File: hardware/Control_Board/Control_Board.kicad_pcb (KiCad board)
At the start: 4 copper layers, 100 x 100 mm, 0 parts

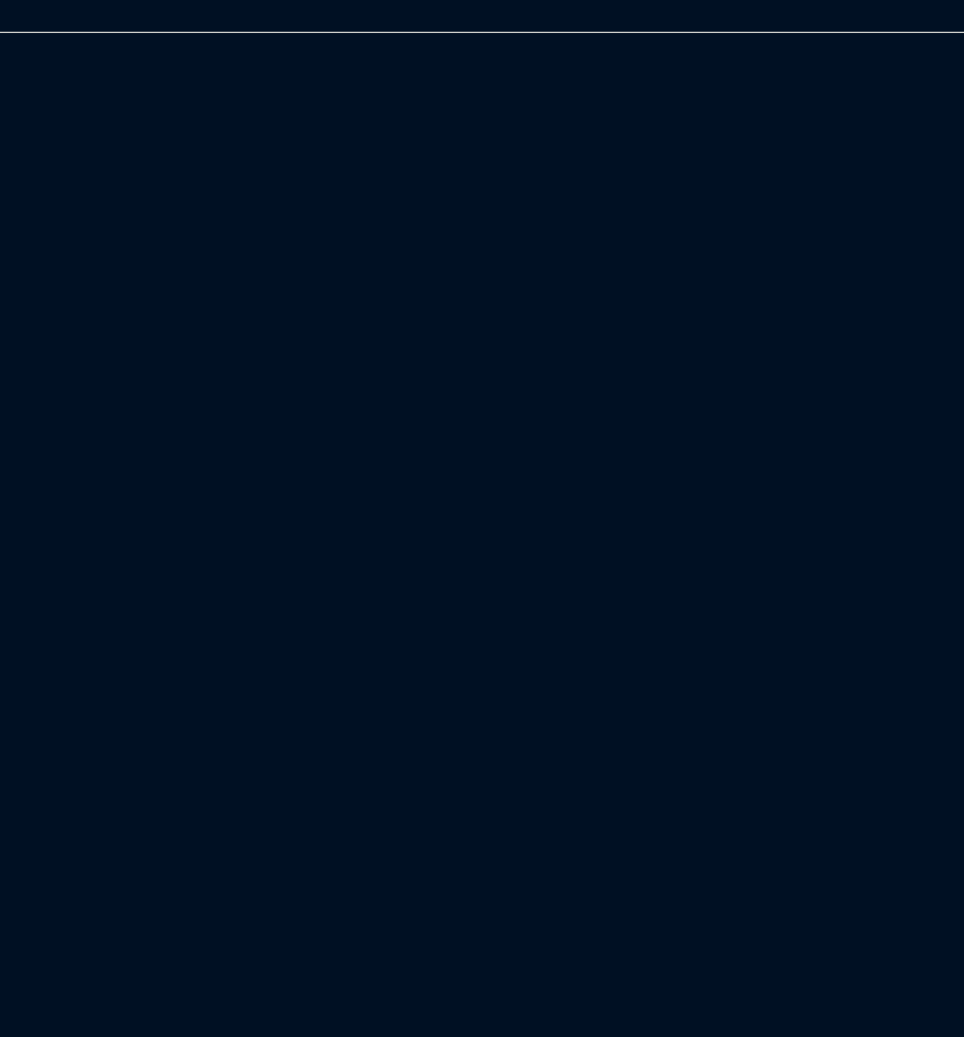
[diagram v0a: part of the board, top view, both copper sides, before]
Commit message: feat: update prototype with esp32
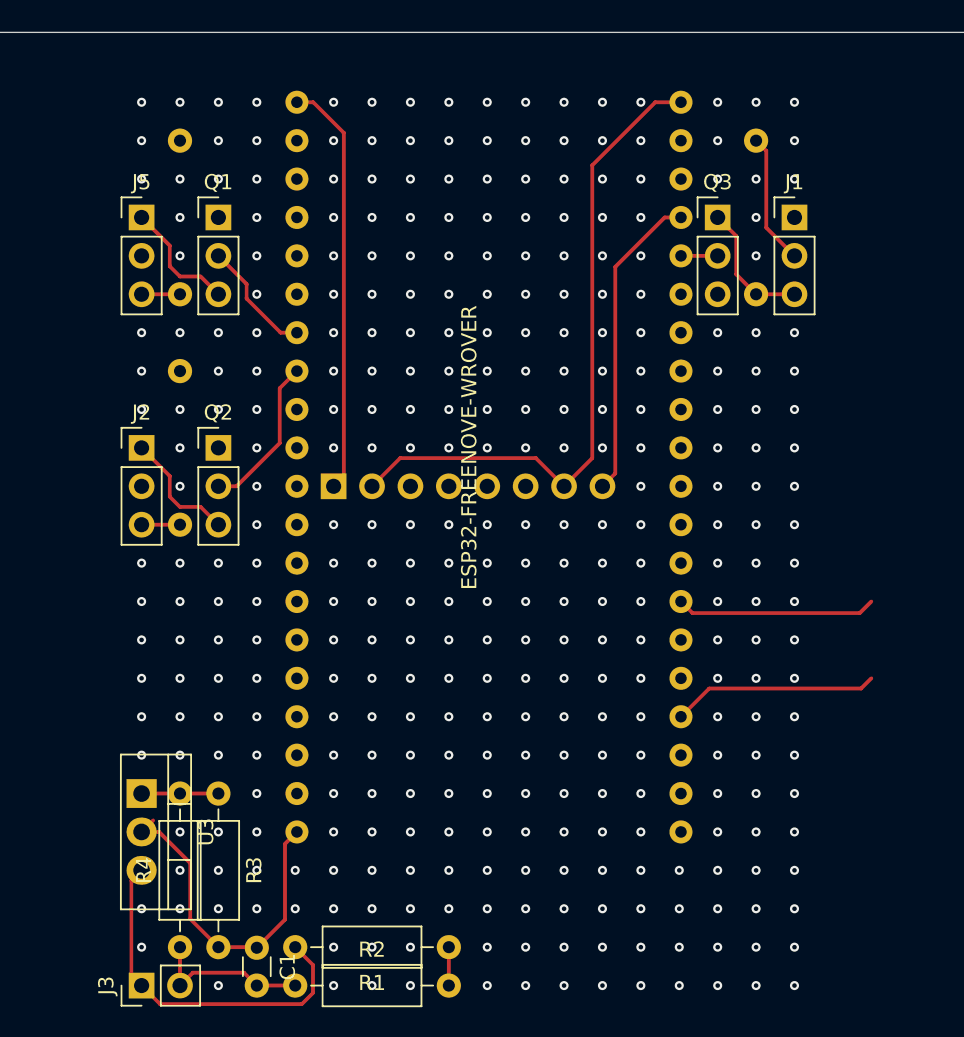
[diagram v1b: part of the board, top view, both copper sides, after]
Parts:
- added C1: 100u, Capacitor_THT:C_Disc_D3.0mm_W1.6mm_P2.50mm, F.Cu at (63.5, 190.5)
- added J1: Left Motor, Connector_PinHeader_2.54mm:PinHeader_1x03_P2.54mm_Vertical, F.Cu at (99.1, 142.2)
- added J2: Right Motor, Connector_PinHeader_2.54mm:PinHeader_1x03_P2.54mm_Vertical, F.Cu at (55.9, 157.5)
- added J3: Battery, Connector_PinHeader_2.54mm:PinHeader_1x02_P2.54mm_Vertical, F.Cu at (55.9, 193.0)
- added J4: MPU-6050, Connector_PinSocket_2.54mm:PinSocket_1x08_P2.54mm_Vertical, B.Cu at (68.6, 160.0)
- added J5: Pitch Motor, Connector_PinHeader_2.54mm:PinHeader_1x03_P2.54mm_Vertical, F.Cu at (55.9, 142.2)
- added Q1: NMOS, Connector_PinHeader_2.54mm:PinHeader_1x03_P2.54mm_Vertical, F.Cu at (61.0, 142.2)
- added Q2: NMOS, Connector_PinHeader_2.54mm:PinHeader_1x03_P2.54mm_Vertical, F.Cu at (61.0, 157.5)
- added Q3: NMOS, Connector_PinHeader_2.54mm:PinHeader_1x03_P2.54mm_Vertical, F.Cu at (94.0, 142.2)
- added R1: 420k, Resistor_THT:R_Axial_DIN0207_L6.3mm_D2.5mm_P10.16mm_Horizontal, F.Cu at (76.2, 190.5)
- added R2: 100k, Resistor_THT:R_Axial_DIN0207_L6.3mm_D2.5mm_P10.16mm_Horizontal, F.Cu at (66.0, 193.0)
- added R3: 1k, Resistor_THT:R_Axial_DIN0207_L6.3mm_D2.5mm_P10.16mm_Horizontal, F.Cu at (61.0, 180.3)
- added R4: 15k, Resistor_THT:R_Axial_DIN0207_L6.3mm_D2.5mm_P10.16mm_Horizontal, F.Cu at (58.4, 190.5)
- added R5: 10k, Resistor_THT:R_Axial_DIN0207_L6.3mm_D2.5mm_P10.16mm_Horizontal, B.Cu at (58.4, 147.3)
- added R6: 10k, Resistor_THT:R_Axial_DIN0207_L6.3mm_D2.5mm_P10.16mm_Horizontal, B.Cu at (58.4, 162.6)
- added R7: 10k, Resistor_THT:R_Axial_DIN0207_L6.3mm_D2.5mm_P10.16mm_Horizontal, B.Cu at (96.5, 147.3)
- added U1: ESP32-FREENOVE-WROVER, PCM_Espressif:ESP32-FREENOVE-WROVER, F.Cu at (64.9, 133.3)
- added U3: LM317_TO-220, Package_TO_SOT_THT:TO-220-3_Vertical, F.Cu at (55.9, 180.3)
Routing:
- net /GND: track 0.00 -> 98.7 mm, vias 0 -> 9
- net /3P3V: track 0.00 -> 27.6 mm, vias 0 -> 2
- net /VBAT: track 0.00 -> 23.8 mm, vias 0 -> 3
- net /5V: track 0.00 -> 22.8 mm, vias 0 -> 4
- net /IMU_INT: track 0.00 -> 20.4 mm, vias 0 -> 2
- net /EXTRA: track 0.00 -> 13.2 mm, vias 0 -> 1
- net /IMU_SDA: track 0.00 -> 13.1 mm, vias 0 -> 2
- net /R_PWM: track 0.00 -> 10.5 mm, vias 0 -> 2
- net /IMU_SCL: track 0.00 -> 9.05 mm, vias 0 -> 2
- net Net-(J5-Pin_2): track 0.00 -> 8.67 mm, vias 0 -> 2
- net Net-(J2-Pin_3): track 0.00 -> 8.67 mm, vias 0 -> 3
- net Net-(J1-Pin_2): track 0.00 -> 8.67 mm, vias 0 -> 2
- net Net-(J2-Pin_2): track 0.00 -> 8.67 mm, vias 0 -> 2
- net Net-(J5-Pin_3): track 0.00 -> 8.67 mm, vias 0 -> 3
- net Net-(J1-Pin_3): track 0.00 -> 8.67 mm, vias 0 -> 3
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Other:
- board text removed: "0.2000 mm / 0.2000 mm"
- board text removed: "0.3000 mm"
- board text removed: "1.6000 mm"
- board text removed: "100.0000 mm x 100.0000 mm"
- board text removed: "4"
- board text removed: "BOARD CHARACTERISTICS"
- board text removed: "Board Thickness:"
- board text removed: "Board overall dimensions:"
- board text removed: "Castellated pads:"
- board text removed: "Copper Finish:"
- board text removed: "Copper Layer Count:"
- board text removed: "ENIG"
- board text removed: "Edge card connectors:"
- board text removed: "Impedance Control:"
- board text removed: "Min hole diameter:"
- board text removed: "Min track/spacing:"
- board text removed: "Netclasses are calculated for current board stackup which corrisponds to the standard 4 layer from PCBWay"
- board text removed: "No"
- board text removed: "Plated Board Edge:"
